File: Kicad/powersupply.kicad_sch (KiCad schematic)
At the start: 26 parts, among them J1301 Jack 2.1{slash}6.3mm, J1302 Conn_02x02S, J1303 Conn_01x04S, Q1301 AO3401A, Q1302 SS8550, Q1303 SS8050, U1301 DC-DC Module, U1302 AMS1117-3.3, U1303 HT75xx-1-SOT89

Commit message: Label adjustments.
Swap 10uF to 10u (the F is implied)
Adjust some left/right alignment and nudge some labels around
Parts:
- C1301, C1302: value 100uF -> 100u
- C1303, C1304, C1305: value 22uF -> 22u
- C1306, C1307: value 10uF -> 10u
- J1301: value Jack 2.1/6.3mm -> Jack 2.1mm 6.3mm
- U1303: LSCS Part# C14289 -> (none)
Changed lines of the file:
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@@
   )
   (text "~{SHDN} must be low at power-up to avoid\nDC-DC enabling temporarily. To do this\nQx01 is an open-collector switch, driving\na PNP (high-side output) inverter.\n\nTo activate PSU, ~{SHDN} must be raised to\nbetween 4.5V and 14V. We use a Zener to\nclamp VDC as we have no other suitable\nvoltage source available (the microLDO is\n3.3V).\n\nRaising DC_ON to above 0.7V will switch on\nQx01. This will allow current to flow through\nthe base of Qx02 to GND, switching on current\nthrough Qx02, which will raise ~{SHDN} to\na suitable level.\n\nThe CTRL pin on the DCDC PSU has high\ninput impedance so no current limiting\nresistor is required."
-    (at 94.615 163.195 0)
+    (at 100.33 168.275 0)
     (effects (font (size 1.27 1.27) italic) (justify left bottom))
   )
@@
       (effects (font (size 1.27 1.27)) (justify left))
     )
-    (property "Value" "100uF" (id 1) (at 81.28 66.675 0)
+    (property "Value" "100u" (id 1) (at 81.28 66.675 0)
       (effects (font (size 1.27 1.27)) (justify left))
     )
@@
       (effects (font (size 1.27 1.27)) (justify left))
     )
-    (property "Value" "100uF" (id 1) (at 93.98 66.675 0)
+    (property "Value" "100u" (id 1) (at 93.98 66.675 0)
       (effects (font (size 1.27 1.27)) (justify left))
     )
@@
     (in_bom yes) (on_board yes)
     (property "Reference" "J1301" (id 0) (at 33.02 47.625 0))
-    (property "Value" "Jack 2.1{slash}6.3mm" (id 1) (at 33.02 50.165 0))
+    (property "Value" "Jack 2.1mm 6.3mm" (id 1) (at 33.02 50.165 0))
     (property "Footprint" "Connector_BarrelJack:BarrelJack_CUI_PJ-063AH_Horizontal" (id 2) (at 34.29 57.531 0)
       (effects (font (size 1.27 1.27)) hide)
@@
       (effects (font (size 1.27 1.27)) (justify left))
     )
-    (property "Value" "22uF" (id 1) (at 138.2522 65.278 0)
+    (property "Value" "22u" (id 1) (at 138.2522 65.278 0)
       (effects (font (size 1.27 1.27)) (justify left))
     )
@@
   (symbol (lib_id "Device:R") (at 60.325 106.045 270) (mirror x) (unit 1)
     (in_bom yes) (on_board yes)
-    (property "Reference" "R1302" (id 0) (at 57.785 102.235 90)
-      (effects (font (size 1.27 1.27)) (justify left))
-    )
-    (property "Value" "10k" (id 1) (at 58.42 104.14 90)
-      (effects (font (size 1.27 1.27)) (justify left))
-    )
+    (property "Reference" "R1302" (id 0) (at 60.325 103.505 90))
+    (property "Value" "10k" (id 1) (at 60.325 108.585 90))
     (property "Footprint" "Resistor_SMD:R_0805_2012Metric_Pad1.20x1.40mm_HandSolder" (id 2) (at 60.325 107.823 90)
       (effects (font (size 1.27 1.27)) hide)
@@
   (symbol (lib_id "Diode:ZMMxx") (at 88.265 121.285 90) (mirror x) (unit 1)
     (in_bom yes) (on_board yes)
-    (property "Reference" "D1302" (id 0) (at 86.36 120.015 90)
-      (effects (font (size 1.27 1.27)) (justify left))
-    )
-    (property "Value" "ZMM5V6" (id 1) (at 86.36 122.555 90)
-      (effects (font (size 1.27 1.27)) (justify left))
+    (property "Reference" "D1302" (id 0) (at 90.17 120.015 90)
+      (effects (font (size 1.27 1.27)) (justify right))
+    )
+    (property "Value" "ZMM5V6" (id 1) (at 90.17 122.555 90)
+      (effects (font (size 1.27 1.27)) (justify right))
     )
     (property "Footprint" "Diode_SMD:D_MiniMELF" (id 2) (at 92.71 121.285 0)
@@
       (effects (font (size 1.27 1.27)) hide)
     )
-    (property "LSCS Part#" "C14289" (id 4) (at 158.75 101.6 0)
-      (effects (font (size 1.27 1.27)) hide)
-    )
     (property "DNP" "0" (id 5) (at 158.75 101.6 0)
       (effects (font (size 1.27 1.27)) hide)
@@
   (symbol (lib_id "Device:R") (at 82.55 114.935 270) (mirror x) (unit 1)
     (in_bom yes) (on_board yes)
-    (property "Reference" "R1304" (id 0) (at 82.55 111.125 90))
-    (property "Value" "1k" (id 1) (at 82.55 113.03 90))
+    (property "Reference" "R1304" (id 0) (at 82.55 112.395 90))
+    (property "Value" "1k" (id 1) (at 82.55 117.475 90))
     (property "Footprint" "Resistor_SMD:R_0805_2012Metric_Pad1.20x1.40mm_HandSolder" (id 2) (at 82.55 116.713 90)
       (effects (font (size 1.27 1.27)) hide)
@@
       (effects (font (size 1.27 1.27)) (justify left))
     )
-    (property "Value" "22uF" (id 1) (at 212.5472 65.278 0)
+    (property "Value" "22u" (id 1) (at 212.5472 65.278 0)
       (effects (font (size 1.27 1.27)) (justify left))
     )
@@
       (effects (font (size 1.27 1.27)) (justify left))
     )
-    (property "Value" "10uF" (id 1) (at 151.13 107.95 0)
+    (property "Value" "10u" (id 1) (at 151.13 107.95 0)
       (effects (font (size 1.27 1.27)) (justify right))
     )
@@
       (effects (font (size 1.27 1.27)) (justify left))
     )
-    (property "Value" "22uF" (id 1) (at 188.7728 65.278 0)
+    (property "Value" "22u" (id 1) (at 188.7728 65.278 0)
       (effects (font (size 1.27 1.27)) (justify left))
     )
@@
       (effects (font (size 1.27 1.27)) (justify left))
     )
-    (property "Value" "10uF" (id 1) (at 180.975 107.95 0)
+    (property "Value" "10u" (id 1) (at 180.975 107.95 0)
       (effects (font (size 1.27 1.27)) (justify right))
     )

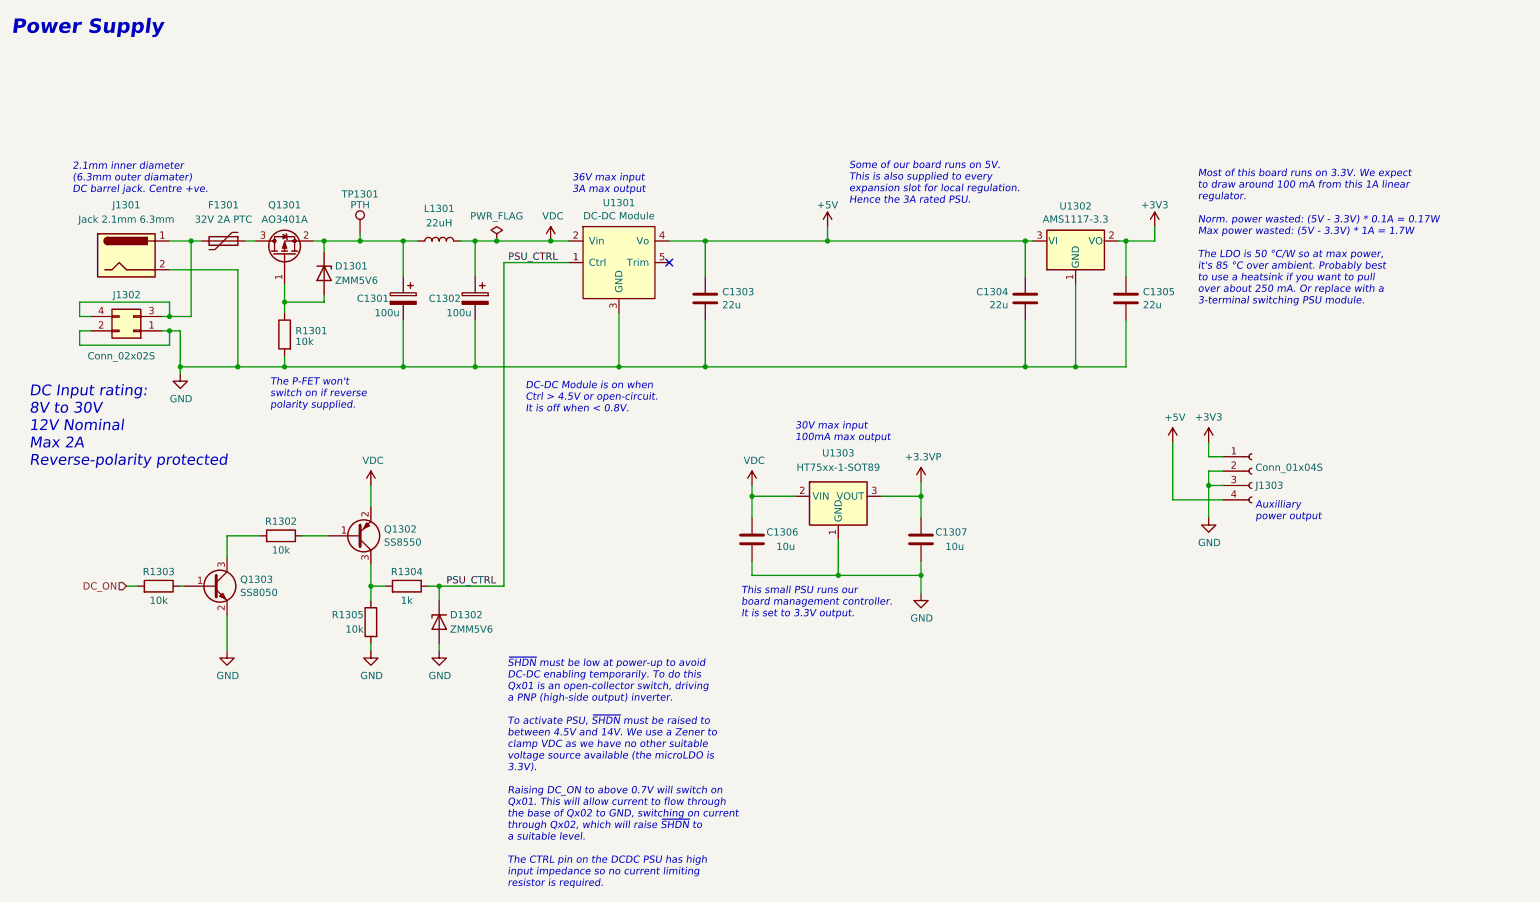
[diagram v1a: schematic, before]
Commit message: Updated to KiCAD 7.
Had to move a net-tie to resolve a "too close" error.
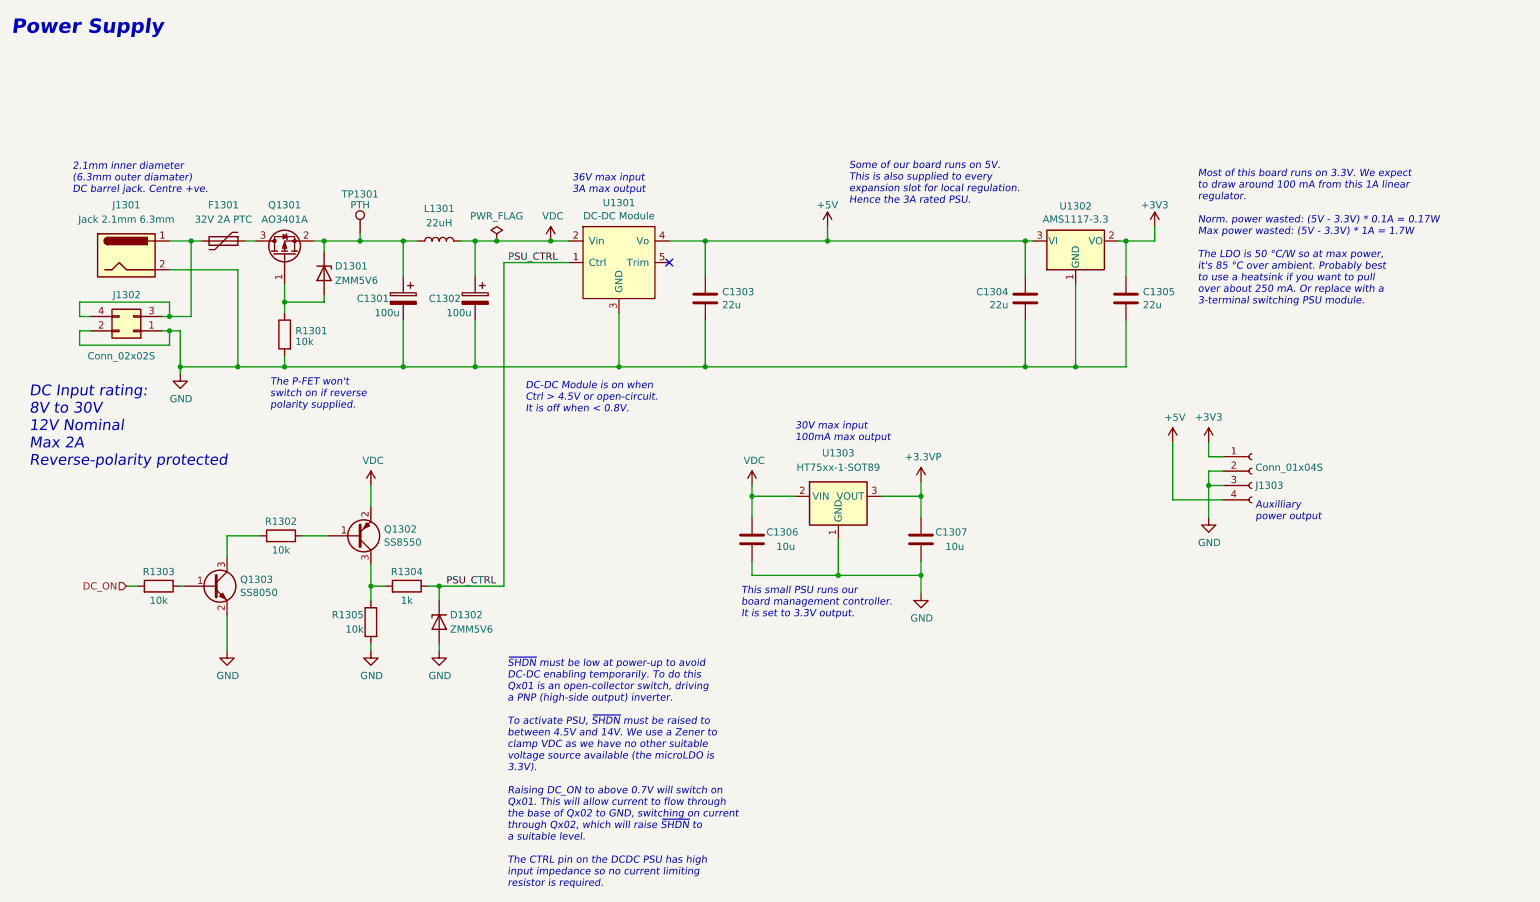
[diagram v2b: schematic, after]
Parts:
- F1301: footprint neotron-pico:Bel Fuse 0ZRS0200FF -> Neotron-Common-Hardware:Bel Fuse 0ZRS0200FF
- J1303: symbol Connector:Conn_01x04_Female -> Connector:Conn_01x04_Socket
